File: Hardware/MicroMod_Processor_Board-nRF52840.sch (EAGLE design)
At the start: 24 parts, among them J1 MICROMOD-2222, U1 W25QXX128MBIT-6X5, U2 MDBT50Q, Y1 32.768kHz

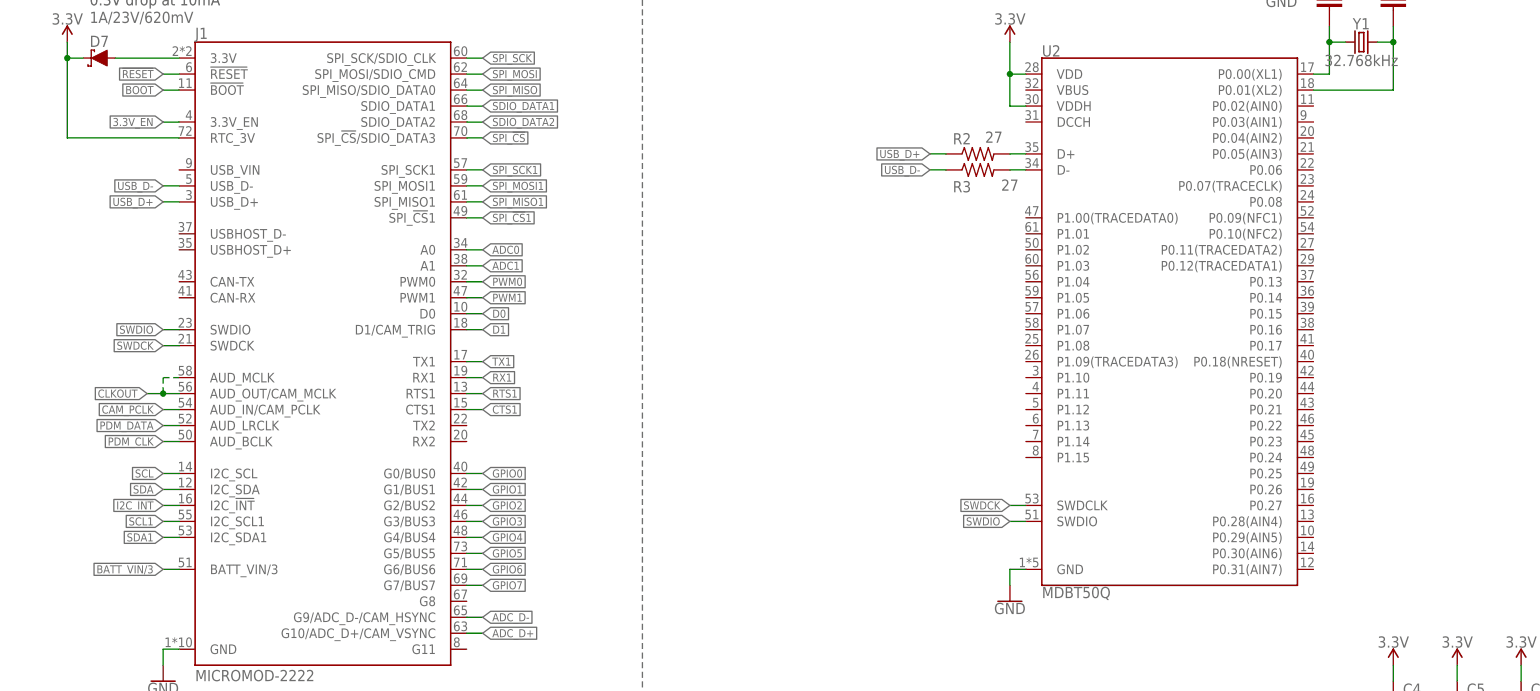
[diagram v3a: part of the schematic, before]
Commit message: Determined nets of some nRF pins.
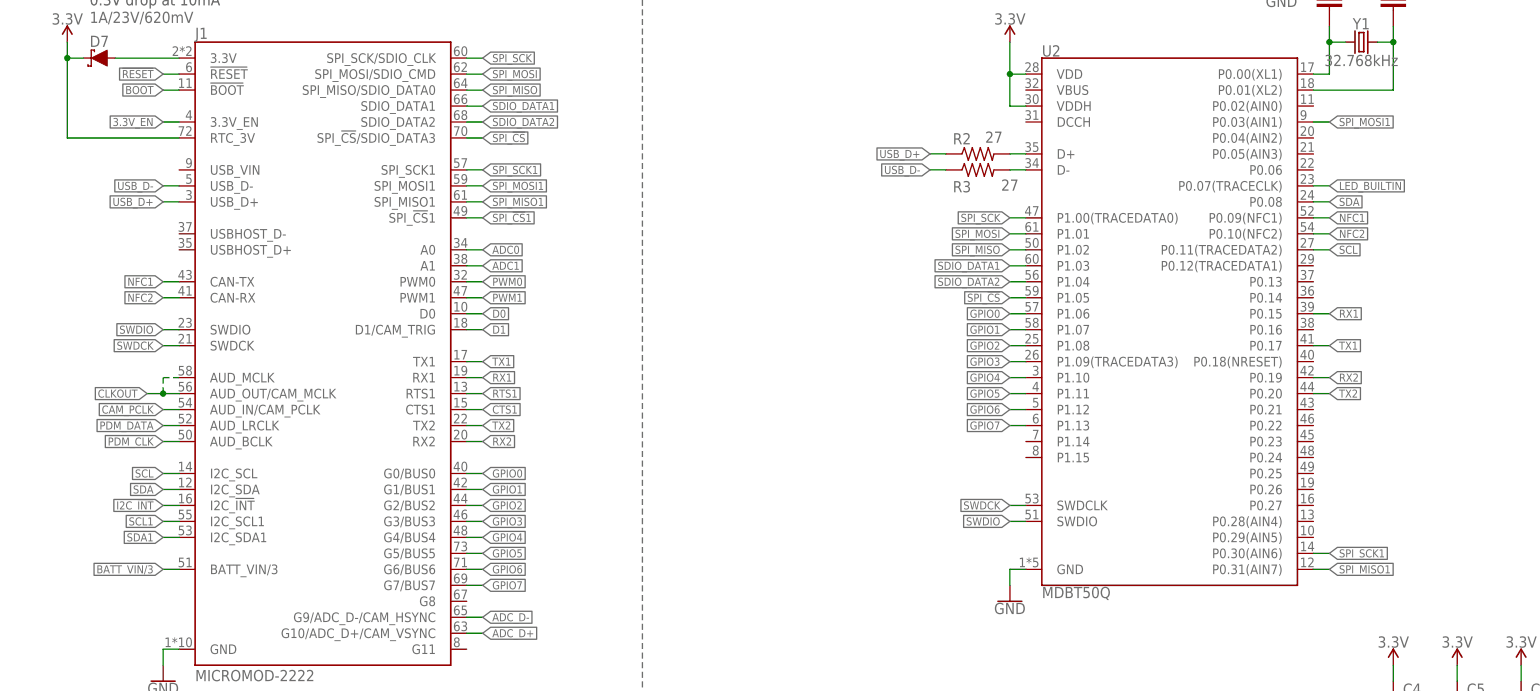
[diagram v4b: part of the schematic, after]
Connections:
- new net NFC1: J1.CAN-TX, U2.P0.09(NFC1)
- new net NFC2: J1.CAN-RX, U2.P0.10(NFC2)
- new net RX2: J1.RX2, U2.P0.19
- new net TX2: J1.TX2, U2.P0.20
- net GPIO0: now also U2.P1.06
- net GPIO1: now also U2.P1.07
- net GPIO2: now also U2.P1.08
- net GPIO3: now also U2.P1.09(TRACEDATA3)
- net GPIO4: now also U2.P1.10
- net GPIO5: now also U2.P1.11
- net GPIO6: now also U2.P1.12
- net GPIO7: now also U2.P1.13
- net LED_BUILTIN: now also U2.P0.07(TRACECLK)
- net RX1: now also U2.P0.15
- net SCL: now also U2.P0.11(TRACEDATA2)
- net SDA: now also U2.P0.08
- net SDIO_DATA1: now also U2.P1.03
- net SDIO_DATA2: now also U2.P1.04
- net SPI_!CS!: now also U2.P1.05
- net SPI_MISO: now also U2.P1.02
- net SPI_MISO1: now also U2.P0.31(AIN7)
- net SPI_MOSI: now also U2.P1.01
- net SPI_MOSI1: now also U2.P0.03(AIN1)
- net SPI_SCK: now also U2.P1.00(TRACEDATA0)
- net SPI_SCK1: now also U2.P0.30(AIN6)
- net TX1: now also U2.P0.17
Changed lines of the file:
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@@
 <?xml version="1.0" encoding="utf-8"?>
 <!DOCTYPE eagle SYSTEM "eagle.dtd">
-<eagle version="9.4.2">
+<eagle version="9.5.2">
 <drawing>
 <settings>
-<setting alwaysvectorfont="yes"/>
+<setting alwaysvectorfont="no"/>
 <setting verticaltext="up"/>
 </settings>
@@
 <pinref part="J1" gate="J1" pin="SPI_SCK1"/>
 </segment>
+<segment>
+<pinref part="U2" gate="G$1" pin="P0.30(AIN6)"/>
+<wire x1="210.82" y1="175.26" x2="213.36" y2="175.26" width="0.1524" layer="91"/>
+<label x="213.36" y="175.26" size="1.27" layer="95" xref="yes"/>
+</segment>
 </net>
 <net name="SPI_MOSI1" class="0">
@@
 <pinref part="J1" gate="J1" pin="SPI_MOSI1"/>
 </segment>
+<segment>
+<pinref part="U2" gate="G$1" pin="P0.03(AIN1)"/>
+<wire x1="210.82" y1="243.84" x2="213.36" y2="243.84" width="0.1524" layer="91"/>
+<label x="213.36" y="243.84" size="1.27" layer="95" xref="yes"/>
+</segment>
 </net>
 <net name="TX1" class="0">
@@
 <pinref part="J1" gate="J1" pin="TX1"/>
 </segment>
+<segment>
+<pinref part="U2" gate="G$1" pin="P0.17"/>
+<wire x1="210.82" y1="208.28" x2="213.36" y2="208.28" width="0.1524" layer="91"/>
+<label x="213.36" y="208.28" size="1.27" layer="95" xref="yes"/>
+</segment>
 </net>
 <net name="RX1" class="0">
@@
 <pinref part="J1" gate="J1" pin="RX1"/>
 </segment>
+<segment>
+<pinref part="U2" gate="G$1" pin="P0.15"/>
+<wire x1="210.82" y1="213.36" x2="213.36" y2="213.36" width="0.1524" layer="91"/>
+<label x="213.36" y="213.36" size="1.27" layer="95" xref="yes"/>
+</segment>
 </net>
 <net name="I2C_!INT!" class="0">
@@
 <pinref part="J1" gate="J1" pin="I2C_SCL"/>
 </segment>
+<segment>
+<pinref part="U2" gate="G$1" pin="P0.11(TRACEDATA2)"/>
+<wire x1="210.82" y1="223.52" x2="213.36" y2="223.52" width="0.1524" layer="91"/>
+<label x="213.36" y="223.52" size="1.27" layer="95" xref="yes"/>
+</segment>
 </net>
 <net name="SDA" class="0">
@@
 <pinref part="J1" gate="J1" pin="I2C_SDA"/>
 </segment>
+<segment>
+<pinref part="U2" gate="G$1" pin="P0.08"/>
+<wire x1="210.82" y1="231.14" x2="213.36" y2="231.14" width="0.1524" layer="91"/>
+<label x="213.36" y="231.14" size="1.27" layer="95" xref="yes"/>
+</segment>
 </net>
 <net name="PDM_DATA" class="0">
@@
 <pinref part="J1" gate="J1" pin="SPI_SCK/SDIO_CLK"/>
 </segment>
+<segment>
+<pinref part="U2" gate="G$1" pin="P1.00(TRACEDATA0)"/>
+<wire x1="165.1" y1="228.6" x2="162.56" y2="228.6" width="0.1524" layer="91"/>
+<label x="162.56" y="228.6" size="1.27" layer="95" rot="R180" xref="yes"/>
+</segment>
 </net>
 <net name="SPI_MISO" class="0">
@@
 <pinref part="J1" gate="J1" pin="SPI_MISO/SDIO_DATA0"/>
 </segment>
+<segment>
+<pinref part="U2" gate="G$1" pin="P1.02"/>
+<wire x1="165.1" y1="223.52" x2="162.56" y2="223.52" width="0.1524" layer="91"/>
+<label x="162.56" y="223.52" size="1.27" layer="95" rot="R180" xref="yes"/>
+</segment>
 </net>
 <net name="SPI_MOSI" class="0">
@@
 <pinref part="J1" gate="J1" pin="SPI_MOSI/SDIO_CMD"/>
 </segment>
+<segment>
+<pinref part="U2" gate="G$1" pin="P1.01"/>
+<wire x1="165.1" y1="226.06" x2="162.56" y2="226.06" width="0.1524" layer="91"/>
+<label x="162.56" y="226.06" size="1.27" layer="95" rot="R180" xref="yes"/>
+</segment>
 </net>
 <net name="SPI_!CS!" class="0">
@@
 <label x="78.74" y="241.3" size="1.27" layer="95" xref="yes"/>
 <pinref part="J1" gate="J1" pin="SPI_!CS!/SDIO_DATA3"/>
+</segment>
+<segment>
+<pinref part="U2" gate="G$1" pin="P1.05"/>
+<wire x1="165.1" y1="215.9" x2="162.56" y2="215.9" width="0.1524" layer="91"/>
+<label x="162.56" y="215.9" size="1.27" layer="95" rot="R180" xref="yes"/>
 </segment>
 </net>
@@
 <label x="58.42" y="111.76" size="1.27" layer="95" rot="R180" xref="yes"/>
 </segment>
+<segment>
+<pinref part="U2" gate="G$1" pin="P0.07(TRACECLK)"/>
+<wire x1="210.82" y1="233.68" x2="213.36" y2="233.68" width="0.1524" layer="91"/>
+<label x="213.36" y="233.68" size="1.27" layer="95" xref="yes"/>
+</segment>
 </net>
 <net name="SCL1" class="0">
@@
 <pinref part="J1" gate="J1" pin="SDIO_DATA1"/>
 </segment>
+<segment>
+<pinref part="U2" gate="G$1" pin="P1.03"/>
+<wire x1="165.1" y1="220.98" x2="162.56" y2="220.98" width="0.1524" layer="91"/>
+<label x="162.56" y="220.98" size="1.27" layer="95" rot="R180" xref="yes"/>
+</segment>
 </net>
 <net name="SDIO_DATA2" class="0">
@@
 <pinref part="J1" gate="J1" pin="SDIO_DATA2"/>
 </segment>
+<segment>
+<pinref part="U2" gate="G$1" pin="P1.04"/>
+<wire x1="165.1" y1="218.44" x2="162.56" y2="218.44" width="0.1524" layer="91"/>
+<label x="162.56" y="218.44" size="1.27" layer="95" rot="R180" xref="yes"/>
+</segment>
 </net>
 <net name="ADC_D-" class="0">
@@
 <pinref part="J1" gate="J1" pin="SPI_MISO1"/>
 </segment>
+<segment>
+<pinref part="U2" gate="G$1" pin="P0.31(AIN7)"/>
+<wire x1="210.82" y1="172.72" x2="213.36" y2="172.72" width="0.1524" layer="91"/>
+<label x="213.36" y="172.72" size="1.27" layer="95" xref="yes"/>
+</segment>
 </net>
 <net name="CTS1" class="0">
@@
 <pinref part="J1" gate="J1" pin="G5/BUS5"/>
 </segment>
+<segment>
+<pinref part="U2" gate="G$1" pin="P1.11"/>
+<wire x1="165.1" y1="200.66" x2="162.56" y2="200.66" width="0.1524" layer="91"/>
+<label x="162.56" y="200.66" size="1.27" layer="95" rot="R180" xref="yes"/>
+</segment>
 </net>
 <net name="GPIO7" class="0">
@@
 <pinref part="J1" gate="J1" pin="G7/BUS7"/>
 </segment>
+<segment>
+<pinref part="U2" gate="G$1" pin="P1.13"/>
+<wire x1="165.1" y1="195.58" x2="162.56" y2="195.58" width="0.1524" layer="91"/>
+<label x="162.56" y="195.58" size="1.27" layer="95" rot="R180" xref="yes"/>
+</segment>
 </net>
 <net name="GPIO6" class="0">
@@
 <label x="78.74" y="172.72" size="1.27" layer="95" xref="yes"/>
 <pinref part="J1" gate="J1" pin="G6/BUS6"/>
+</segment>
+<segment>
+<pinref part="U2" gate="G$1" pin="P1.12"/>
+<wire x1="165.1" y1="198.12" x2="162.56" y2="198.12" width="0.1524" layer="91"/>
+<label x="162.56" y="198.12" size="1.27" layer="95" rot="R180" xref="yes"/>
 </segment>
 </net>
@@
 <pinref part="J1" gate="J1" pin="G1/BUS1"/>
 </segment>
+<segment>
+<pinref part="U2" gate="G$1" pin="P1.07"/>
+<wire x1="165.1" y1="210.82" x2="162.56" y2="210.82" width="0.1524" layer="91"/>
+<label x="162.56" y="210.82" size="1.27" layer="95" rot="R180" xref="yes"/>
+</segment>
 </net>
 <net name="GPIO3" class="0">
@@
 <pinref part="J1" gate="J1" pin="G3/BUS3"/>
 </segment>
+<segment>
+<pinref part="U2" gate="G$1" pin="P1.09(TRACEDATA3)"/>
+<wire x1="165.1" y1="205.74" x2="162.56" y2="205.74" width="0.1524" layer="91"/>
+<label x="162.56" y="205.74" size="1.27" layer="95" rot="R180" xref="yes"/>
+</segment>
 </net>
 <net name="GPIO2" class="0">
@@
 <pinref part="J1" gate="J1" pin="G2/BUS2"/>
 </segment>
+<segment>
+<pinref part="U2" gate="G$1" pin="P1.08"/>
+<wire x1="165.1" y1="208.28" x2="162.56" y2="208.28" width="0.1524" layer="91"/>
+<label x="162.56" y="208.28" size="1.27" layer="95" rot="R180" xref="yes"/>
+</segment>
 </net>
 <net name="GPIO4" class="0">
@@
 <pinref part="J1" gate="J1" pin="G4/BUS4"/>
 </segment>
+<segment>
+<pinref part="U2" gate="G$1" pin="P1.10"/>
+<wire x1="165.1" y1="203.2" x2="162.56" y2="203.2" width="0.1524" layer="91"/>
+<label x="162.56" y="203.2" size="1.27" layer="95" rot="R180" xref="yes"/>
+</segment>
 </net>
 <net name="GPIO0" class="0">
@@
 <label x="78.74" y="187.96" size="1.27" layer="95" xref="yes"/>
 <pinref part="J1" gate="J1" pin="G0/BUS0"/>
+</segment>
+<segment>
+<pinref part="U2" gate="G$1" pin="P1.06"/>
+<wire x1="165.1" y1="213.36" x2="162.56" y2="213.36" width="0.1524" layer="91"/>
+<label x="162.56" y="213.36" size="1.27" layer="95" rot="R180" xref="yes"/>
 </segment>
 </net>
@@
 </segment>
 </net>
+<net name="NFC1" class="0">
+<segment>
+<pinref part="U2" gate="G$1" pin="P0.09(NFC1)"/>
+<wire x1="210.82" y1="228.6" x2="213.36" y2="228.6" width="0.1524" layer="91"/>
+<label x="213.36" y="228.6" size="1.27" layer="95" xref="yes"/>
+</segment>
+<segment>
+<pinref part="J1" gate="J1" pin="CAN-TX"/>
+<wire x1="30.48" y1="218.44" x2="27.94" y2="218.44" width="0.1524" layer="91"/>
+<label x="27.94" y="218.44" size="1.27" layer="95" rot="R180" xref="yes"/>
+</segment>
+</net>
+<net name="NFC2" class="0">
+<segment>
+<pinref part="U2" gate="G$1" pin="P0.10(NFC2)"/>
+<wire x1="210.82" y1="226.06" x2="213.36" y2="226.06" width="0.1524" layer="91"/>
+<label x="213.36" y="226.06" size="1.27" layer="95" xref="yes"/>
+</segment>
+<segment>
+<pinref part="J1" gate="J1" pin="CAN-RX"/>
+<wire x1="30.48" y1="215.9" x2="27.94" y2="215.9" width="0.1524" layer="91"/>
+<label x="27.94" y="215.9" size="1.27" layer="95" rot="R180" xref="yes"/>
+</segment>
+</net>
+<net name="RX2" class="0">
+<segment>
+<pinref part="U2" gate="G$1" pin="P0.19"/>
+<wire x1="210.82" y1="203.2" x2="213.36" y2="203.2" width="0.1524" layer="91"/>
+<label x="213.36" y="203.2" size="1.27" layer="95" xref="yes"/>
+</segment>
+<segment>
+<pinref part="J1" gate="J1" pin="RX2"/>
+<wire x1="76.2" y1="193.04" x2="78.74" y2="193.04" width="0.1524" layer="91"/>
+<label x="78.74" y="193.04" size="1.27" layer="95" xref="yes"/>
+</segment>
+</net>
+<net name="TX2" class="0">
+<segment>
+<pinref part="U2" gate="G$1" pin="P0.20"/>
+<wire x1="210.82" y1="200.66" x2="213.36" y2="200.66" width="0.1524" layer="91"/>
+<label x="213.36" y="200.66" size="1.27" layer="95" xref="yes"/>
+</segment>
+<segment>
+<pinref part="J1" gate="J1" pin="TX2"/>
+<wire x1="76.2" y1="195.58" x2="78.74" y2="195.58" width="0.1524" layer="91"/>
+<label x="78.74" y="195.58" size="1.27" layer="95" xref="yes"/>
+</segment>
+</net>

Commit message: Working on schematic
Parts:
- removed D7: 1A/23V/620mV, SparkFun-DiscreteSemi:DIODE-SCHOTTKY-BAT20J
- renumbered J1 to J2
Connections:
- removed net 3.3V_MAIN: D7.A, J2.3.3V
- removed net CAM_PCLK: J2.AUD_IN/CAM_PCLK
- removed net CLKOUT: J2.AUD_MCLK, J2.AUD_OUT/CAM_MCLK
- new net N$6: U1.!CS!
- new net USB_VIN: J2.USB_VIN, U2.VBUS
- net 3.3V: now also J2.3.3V; no longer D7.C, J2.RTC_3V
- net ADC0: now also U2.P0.04(AIN2)
- net ADC1: now also U2.P0.05(AIN3)
- net ADC_D+: now also U2.P0.28(AIN4)
- net ADC_D-: now also U2.P0.02(AIN0)
- net BATT_VIN/3: now also U2.P0.29(AIN5)
- net CTS1: now also U2.P0.06
- net D0: now also U2.P0.27
- net D1: now also U2.P1.08
- net GPIO0: now also U2.P1.15; no longer U2.P1.06
- net GPIO1: now also U2.P1.14; no longer U2.P1.07
- net GPIO2: now also U2.P1.13; no longer U2.P1.08
- net GPIO3: now also U2.P1.12; no longer U2.P1.09(TRACEDATA3)
- net GPIO4: now also U2.P1.11; no longer U2.P1.10
- net GPIO5: now also U2.P1.10; no longer U2.P1.11
- net GPIO6: now also U2.P1.06; no longer U2.P1.12
- net GPIO7: now also U2.P1.04; no longer U2.P1.13
- net I2C_!INT!: now also U2.P1.03
- net PDM_CLK: now also U2.P0.25
- net PDM_DATA: now also U2.P1.02
- net PWM0: now also U2.P1.09(TRACEDATA3)
- net PWM1: now also U2.P0.16
- net RTS1: now also U2.P0.26
- net RX2: now also U2.P1.05; no longer U2.P0.19
- net SCL1: now also U2.P0.24
- net SDA1: now also U2.P1.01
- net SDIO_DATA1: now also U1.D1/DO, U2.P0.22; no longer U2.P1.03
- net SDIO_DATA2: now also U1.D2/!WP!, U2.P0.23; no longer U2.P1.04
- net SPI_!CS!: now also U1.D3/!HOLD!, U2.P1.00(TRACEDATA0); no longer U2.P1.05
- net SPI_!CS!1: now also U2.P0.20
- net SPI_MISO: now also U1.D0/DI, U2.P0.21; no longer U2.P1.02
- net SPI_MOSI: now also U2.P0.18(NRESET); no longer U2.P1.01
- net SPI_SCK: now also U1.CLK, U2.P0.19; no longer U2.P1.00(TRACEDATA0)
- net TX2: now also U2.P1.07; no longer U2.P0.20
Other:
- moved on the sheet: C1, U1

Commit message: Preliminary schematic finished
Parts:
- added R4, R5: 10k, SparkFun-Resistors:10KOHM-0402T-1/16W-1%
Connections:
- removed net 3.3V_EN: J2.3.3V_EN
- removed net BOOT: J2.!BOOT!
- removed net N$6: U1.!CS!
- new net !BOOT!: J2.!BOOT!, R4.1, U2.P0.13
- new net FLASH_!CS!: U1.!CS!, U2.P0.12(TRACEDATA1)
- net !RESET!: now also R5.1, U2.P0.18(NRESET)
- net 3.3V: now also R4.2, R5.2
- net SPI_MOSI: now also U2.P0.14; no longer U2.P0.18(NRESET)
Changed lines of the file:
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@@
 <part name="SUPPLY6" library="SparkFun-PowerSymbols" deviceset="3.3V" device=""/>
 <part name="J2" library="SparkFun-MicroMod" deviceset="MICROMOD" device="-2222"/>
+<part name="R4" library="SparkFun-Resistors" deviceset="10KOHM" device="-0402T-1/16W-1%" value="10k"/>
+<part name="R5" library="SparkFun-Resistors" deviceset="10KOHM" device="-0402T-1/16W-1%" value="10k"/>
+<part name="SUPPLY7" library="SparkFun-PowerSymbols" deviceset="3.3V" device=""/>
+<part name="SUPPLY8" library="SparkFun-PowerSymbols" deviceset="3.3V" device=""/>
 </parts>
 <sheets>
@@
 <attribute name="VALUE" x="33.02" y="154.94" size="1.778" layer="96"/>
 </instance>
+<instance part="R4" gate="G$1" x="231.14" y="226.06" smashed="yes" rot="R90">
+<attribute name="NAME" x="229.616" y="226.06" size="1.778" layer="95" font="vector" rot="R90" align="bottom-center"/>
+<attribute name="VALUE" x="232.664" y="226.06" size="1.778" layer="96" font="vector" rot="R90" align="top-center"/>
+</instance>
+<instance part="R5" gate="G$1" x="241.3" y="213.36" smashed="yes" rot="R90">
+<attribute name="NAME" x="239.776" y="213.36" size="1.778" layer="95" font="vector" rot="R90" align="bottom-center"/>
+<attribute name="VALUE" x="242.824" y="213.36" size="1.778" layer="96" font="vector" rot="R90" align="top-center"/>
+</instance>
+<instance part="SUPPLY7" gate="G$1" x="231.14" y="233.68" smashed="yes">
+<attribute name="VALUE" x="231.14" y="236.474" size="1.778" layer="96" align="bottom-center"/>
+</instance>
+<instance part="SUPPLY8" gate="G$1" x="241.3" y="220.98" smashed="yes">
+<attribute name="VALUE" x="241.3" y="223.774" size="1.778" layer="96" align="bottom-center"/>
+</instance>
 </instances>
 <busses>
@@
 <wire x1="27.94" y1="254" x2="27.94" y2="256.54" width="0.1524" layer="91"/>
 <pinref part="J2" gate="J1" pin="3.3V"/>
+</segment>
+<segment>
+<pinref part="R4" gate="G$1" pin="2"/>
+<pinref part="SUPPLY7" gate="G$1" pin="3.3V"/>
+<wire x1="231.14" y1="233.68" x2="231.14" y2="231.14" width="0.1524" layer="91"/>
+</segment>
+<segment>
+<pinref part="R5" gate="G$1" pin="2"/>
+<pinref part="SUPPLY8" gate="G$1" pin="3.3V"/>
+<wire x1="241.3" y1="220.98" x2="241.3" y2="218.44" width="0.1524" layer="91"/>
 </segment>
 </net>
@@
 <pinref part="J2" gate="J1" pin="!RESET!"/>
 </segment>
-</net>
-<net name="BOOT" class="0">
+<segment>
+<pinref part="U2" gate="G$1" pin="P0.18(NRESET)"/>
+<pinref part="R5" gate="G$1" pin="1"/>
+<wire x1="210.82" y1="205.74" x2="241.3" y2="205.74" width="0.1524" layer="91"/>
+<wire x1="241.3" y1="205.74" x2="241.3" y2="208.28" width="0.1524" layer="91"/>
+<wire x1="241.3" y1="205.74" x2="238.76" y2="205.74" width="0.1524" layer="91"/>
+<junction x="241.3" y="205.74"/>
+<wire x1="241.3" y1="205.74" x2="243.84" y2="205.74" width="0.1524" layer="91"/>
+<label x="243.84" y="205.74" size="1.27" layer="95" xref="yes"/>
+</segment>
+</net>
+<net name="!BOOT!" class="0">
 <segment>
 <wire x1="30.48" y1="248.92" x2="27.94" y2="248.92" width="0.1524" layer="91"/>
@@
 <pinref part="J2" gate="J1" pin="!BOOT!"/>
 </segment>
+<segment>
+<pinref part="U2" gate="G$1" pin="P0.13"/>
+<wire x1="210.82" y1="218.44" x2="231.14" y2="218.44" width="0.1524" layer="91"/>
+<pinref part="R4" gate="G$1" pin="1"/>
+<wire x1="231.14" y1="218.44" x2="231.14" y2="220.98" width="0.1524" layer="91"/>
+<wire x1="231.14" y1="218.44" x2="233.68" y2="218.44" width="0.1524" layer="91"/>
+<junction x="231.14" y="218.44"/>
+<label x="233.68" y="218.44" size="1.27" layer="95" xref="yes"/>
+</segment>
 </net>
 <net name="SWDIO" class="0">
@@
 </segment>
 <segment>
-<pinref part="U2" gate="G$1" pin="P0.18(NRESET)"/>
-<wire x1="210.82" y1="205.74" x2="213.36" y2="205.74" width="0.1524" layer="91"/>
-<label x="213.36" y="205.74" size="1.27" layer="95" xref="yes"/>
+<pinref part="U2" gate="G$1" pin="P0.14"/>
+<wire x1="210.82" y1="215.9" x2="213.36" y2="215.9" width="0.1524" layer="91"/>
+<label x="213.36" y="215.9" size="1.27" layer="95" xref="yes"/>
 </segment>
 </net>
@@
 <wire x1="165.1" y1="190.5" x2="162.56" y2="190.5" width="0.1524" layer="91"/>
 <label x="162.56" y="190.5" size="1.27" layer="95" rot="R180" xref="yes"/>
-</segment>
-</net>
-<net name="3.3V_EN" class="0">
-<segment>
-<wire x1="30.48" y1="243.84" x2="27.94" y2="243.84" width="0.1524" layer="91"/>
-<label x="27.94" y="243.84" size="1.27" layer="95" rot="R180" xref="yes"/>
-<pinref part="J2" gate="J1" pin="3.3V_EN"/>
 </segment>
 </net>
@@
 </segment>
 </net>
-<net name="N$6" class="0">
+<net name="FLASH_!CS!" class="0">
 <segment>
 <pinref part="U1" gate="U1" pin="!CS!"/>
@@
 <label x="60.96" y="40.64" size="1.27" layer="95" xref="yes"/>
 </segment>
-</net>
+<segment>
+<pinref part="U2" gate="G$1" pin="P0.12(TRACEDATA1)"/>
+<wire x1="210.82" y1="220.98" x2="213.36" y2="220.98" width="0.1524" layer="91"/>
+<label x="213.36" y="220.98" size="1.27" layer="95" xref="yes"/>
+</segment>
+</net>
